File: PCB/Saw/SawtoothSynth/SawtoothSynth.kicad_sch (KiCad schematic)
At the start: 35 parts, among them Q1 SS8550, U1 NE555D, U2 LM358, U3 LM386, U4 L7805, U5 4017

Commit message: Added ESP32 & TFT Display to Schematic
Created footprints and added display and ESP32 to schematic with their respective connections
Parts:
- added RoundDispTFT1: ~, DIsplay:1.28__Round_TFT, symbol Display:1.28{dblquote}_Round_TFT
- added U6: ~, Micro Dev Kits:ESP32-WROOM_Devkit, symbol PCM_Espressif:ESP32-WROOM_Devkit
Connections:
- net +5V: now also RoundDispTFT1.1 (Vcc), U6.2 (VIN)
- net DAC: now also U6.10 (DAC_1/ADC2_CH8/GPIO25)
- net GND: now also RoundDispTFT1.2 (GND), U6.1 (GND), U6.15 (GND), U6.38 (GND), U6.39 (GND_THERMAL)
- net SAWTOOTH_MICRO: now reaches R5.2, R6.1, U2.5 (+)
- net SAWTOOTH_MICRO: now also U6.4 (SENSOR_VP/GPIO36/ADC1_CH0)
- new net SPI_CS: RoundDispTFT1.6 (CS), U6.24 (ADC2_CH2/TOUCH/GPIO2)
- new net SPI_DC: RoundDispTFT1.5 (DC), U6.35 (U0TXD/GPIO1)
- new net SPI_MOSI: RoundDispTFT1.4 (SDA), U6.37 (GPIO23)
- new net SPI_RST: RoundDispTFT1.7 (RST), U6.34 (U0RXD/GPIO3)
- new net SPI_SCK: RoundDispTFT1.3 (SCL), U6.30 (GPIO18)
- new net TOUCH: U6.26 (ADC2_CH0/TOUCH/GPIO4)
- no-connect marks 0 -> 1
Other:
- note added: "2.8" TFT Display"
- note added: "ESP32-WROOM Development Kit"

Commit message: Finished Laying Out Schematic
Added all components, footprints, symbols.

Swapped Voltage Regulator to LD1117S50TR due to smaller footprint
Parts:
- removed C6: 250nF, symbol Device:C_Polarized_Small_US
- removed RV1, RV2: 10K, symbol Device:R_Potentiometer
- removed U4: L7805, symbol Regulator_Linear:L7805
- added C6: 220nF, CustomLibrary:25THV220M8X10.5, symbol CustomLibrary:25THV220M8X10.5
- added C8: 25THV220M8X10.5, CAP_J-V_8X10P5_RUB, symbol CustomLibrary:25THV220M8X10.5
- added RV1, RV2: 10K, CustomLibrary:TRIM_TC33X-2-103E, symbol CustomLibrary:TRIM_TC33X-2-103E
- added U7: LD1117S50TR_SOT223, Package_TO_SOT_SMD:SOT-223-3_TabPin2, symbol Regulator_Linear:LD1117S50TR_SOT223
- C1: value C_Small -> 100nF; footprint (none) -> Capacitor_SMD:C_0805_2012Metric
- C2, C3, C7: value C_Small -> 10nF; footprint (none) -> Capacitor_SMD:C_0805_2012Metric
- C4: footprint (none) -> Capacitor_SMD:C_0805_2012Metric
- C5: value C_Small -> 47nF; footprint (none) -> Capacitor_SMD:C_0805_2012Metric
- LS1: footprint (none) -> Connector_PinHeader_2.54mm:PinHeader_1x02_P2.54mm_Vertical
- R1: value R_US -> 100; footprint (none) -> Resistor_SMD:R_0805_2012Metric
- R2, R4: value R_US -> 10K; footprint (none) -> Resistor_SMD:R_0805_2012Metric
- R3: value R_US -> 33K; footprint (none) -> Resistor_SMD:R_0805_2012Metric
- R5: value R_US -> 100K; footprint (none) -> Resistor_SMD:R_0805_2012Metric
- R6: value R_US -> 6.8K; footprint (none) -> Resistor_SMD:R_0805_2012Metric
- R7: value R_US -> 10; footprint (none) -> Resistor_SMD:R_0805_2012Metric
- R8: footprint (none) -> Resistor_SMD:R_0805_2012Metric
- RoundDispTFT1: footprint DIsplay:1.28__Round_TFT -> CustomLibrary:1.28___Round_TFT
- U2: footprint (none) -> CustomLibrary:LM358DR2G
- U3: footprint (none) -> CustomLibrary:LM386MX-1NOPB
- U5: footprint (none) -> CustomLibrary:CD4017BM96
- U6: footprint Micro Dev Kits:ESP32-WROOM_Devkit -> CustomLibrary:ESP32-WROOM_Devkit
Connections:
- net +12V: now also U7.3 (VI)
- net GND: now also RV1.3, U7.1 (GND)
- net at U2.6 (-), U2.7: now also RV2.1
- net at U3.3 (+): now also RV2.2
- net at C5.2, U3.5: now also C6.1
- net at LS1.1: now also C6.2
- net at C7.1: now also U7.2 (VO)
- net at R1.2: now also RV1.2

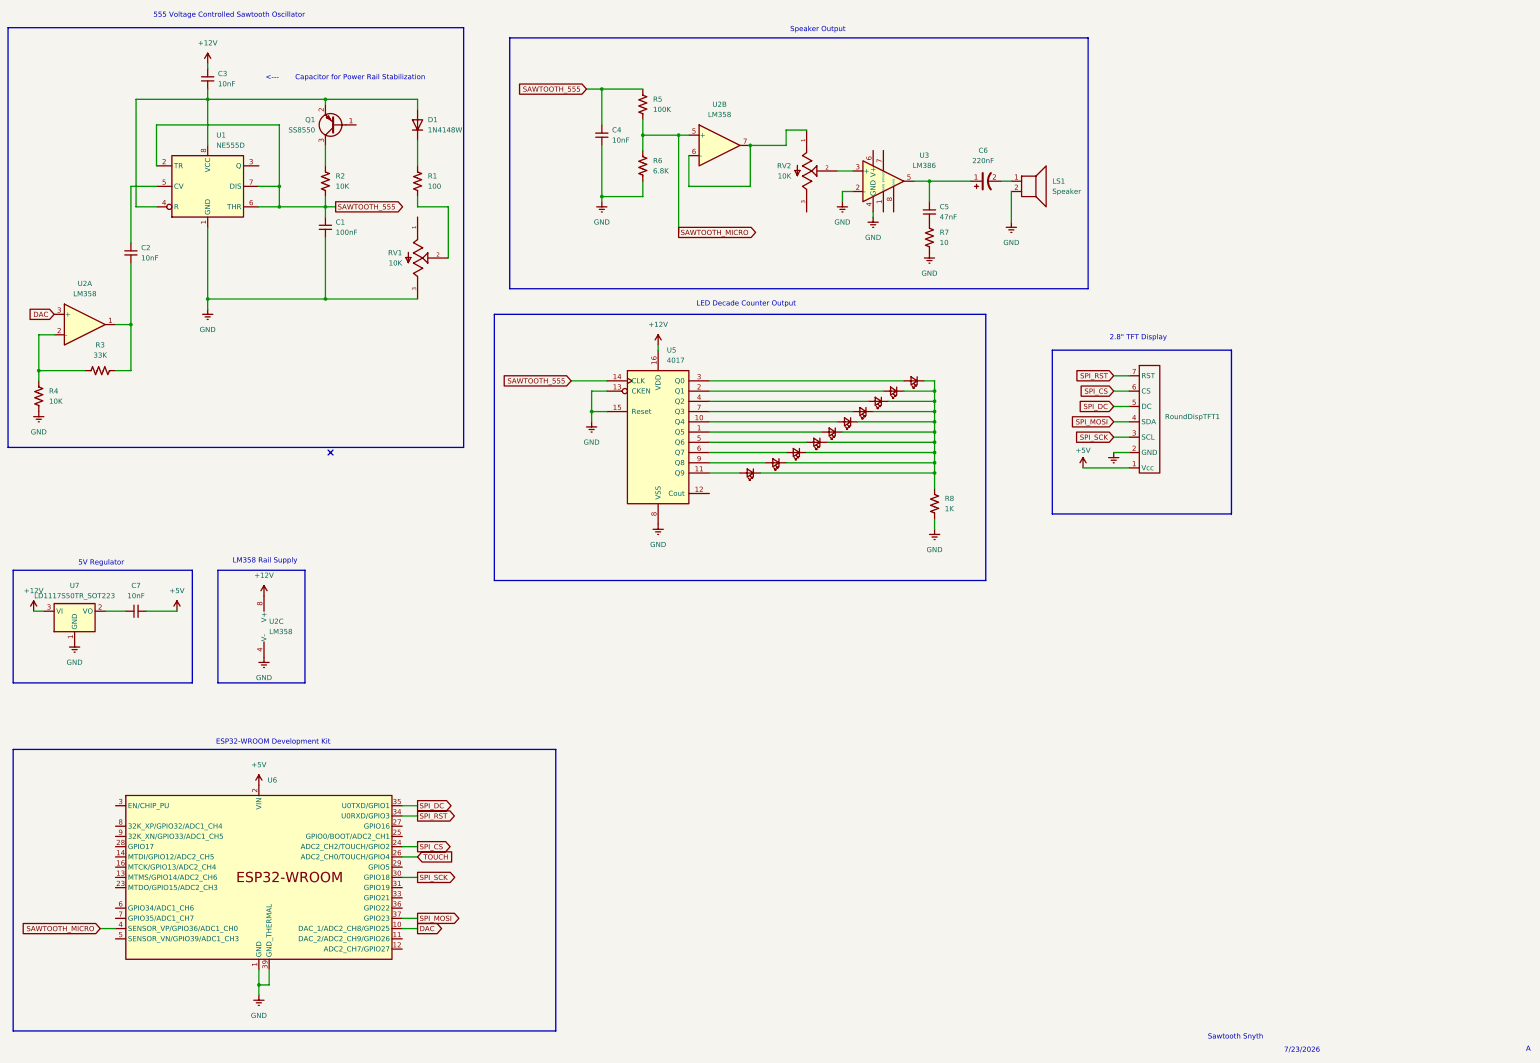
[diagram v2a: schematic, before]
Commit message: Added LED Footprint & Battery Holder
Selected 0805 Footprint for LED and added A23 battery holder to schematic
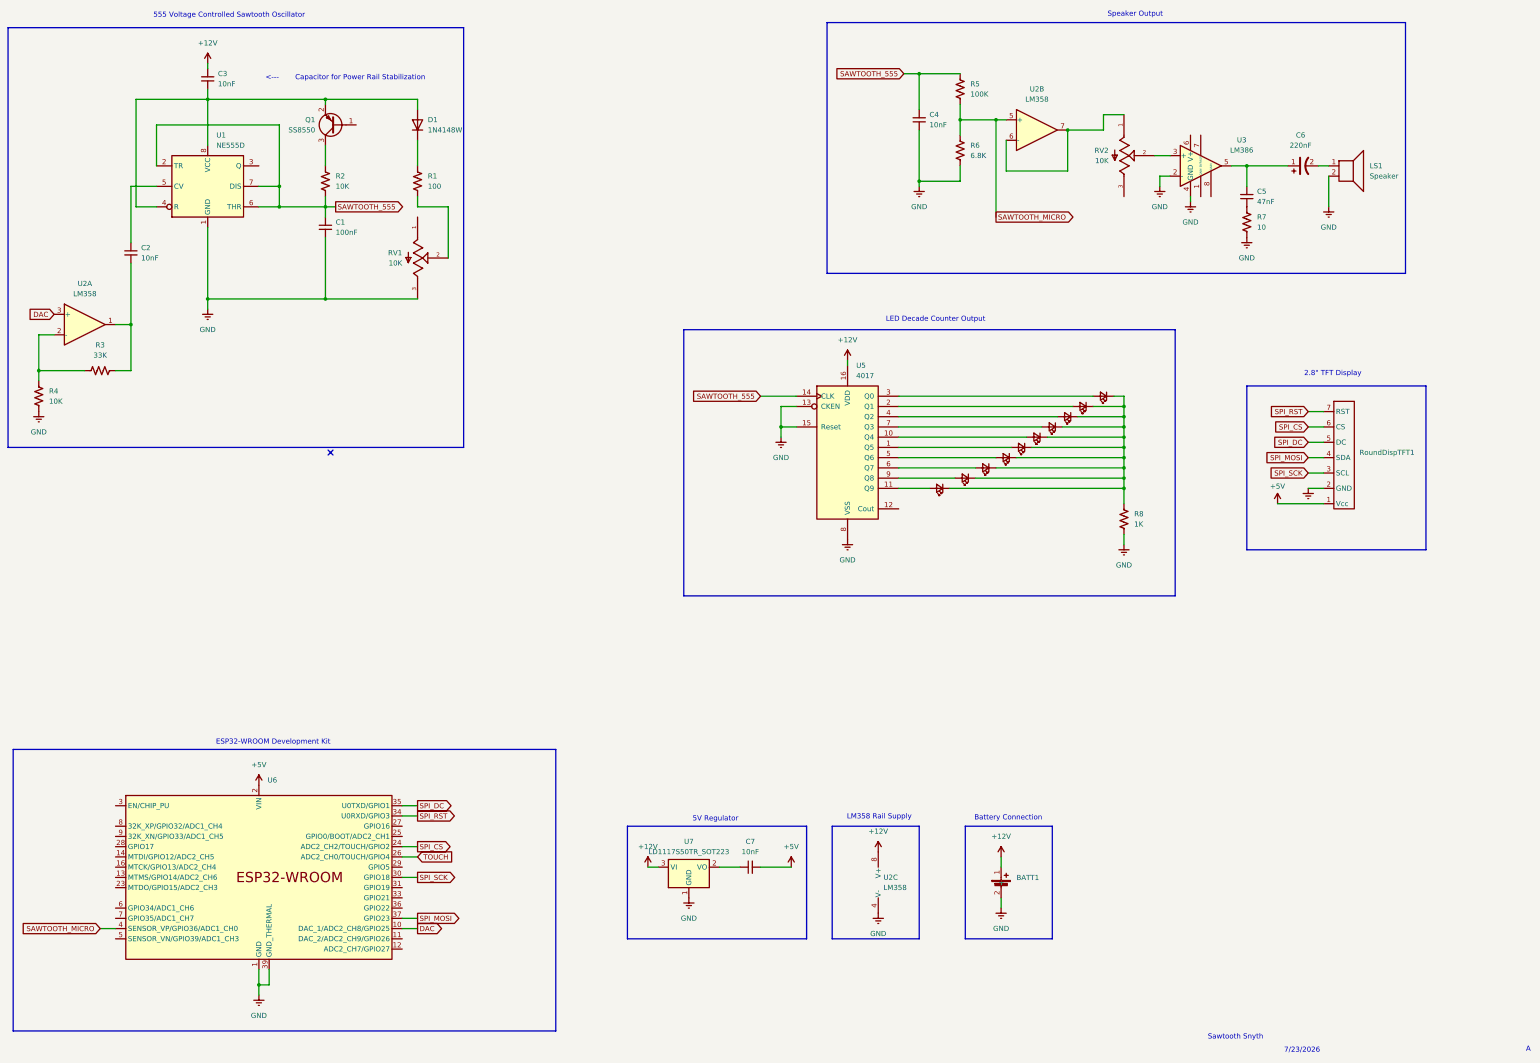
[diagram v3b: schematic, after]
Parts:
- added BATT1: ~, CustomLibrary:BH23APC, symbol CustomLibrary:BH23APC
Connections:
- net +12V: now also BATT1.1 (+)
- net GND: now also BATT1.2 (-)
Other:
- note added: "Battery Connection"
- moved on the sheet: C4, C5, C6, C7, LS1, R5, R6, R7, R8, RV2, RoundDispTFT1, U2B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

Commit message: Created PCB, Updated Schematic
Created an 4 layer, 8 inch PCB
- 2 signal layers, one power, one ground

Last commit I stated that I added the footprint for the LED which was wrong. Updated them correctly in this commit.

Moved capacitor for smoothing the power rail to the positive pin on the battery
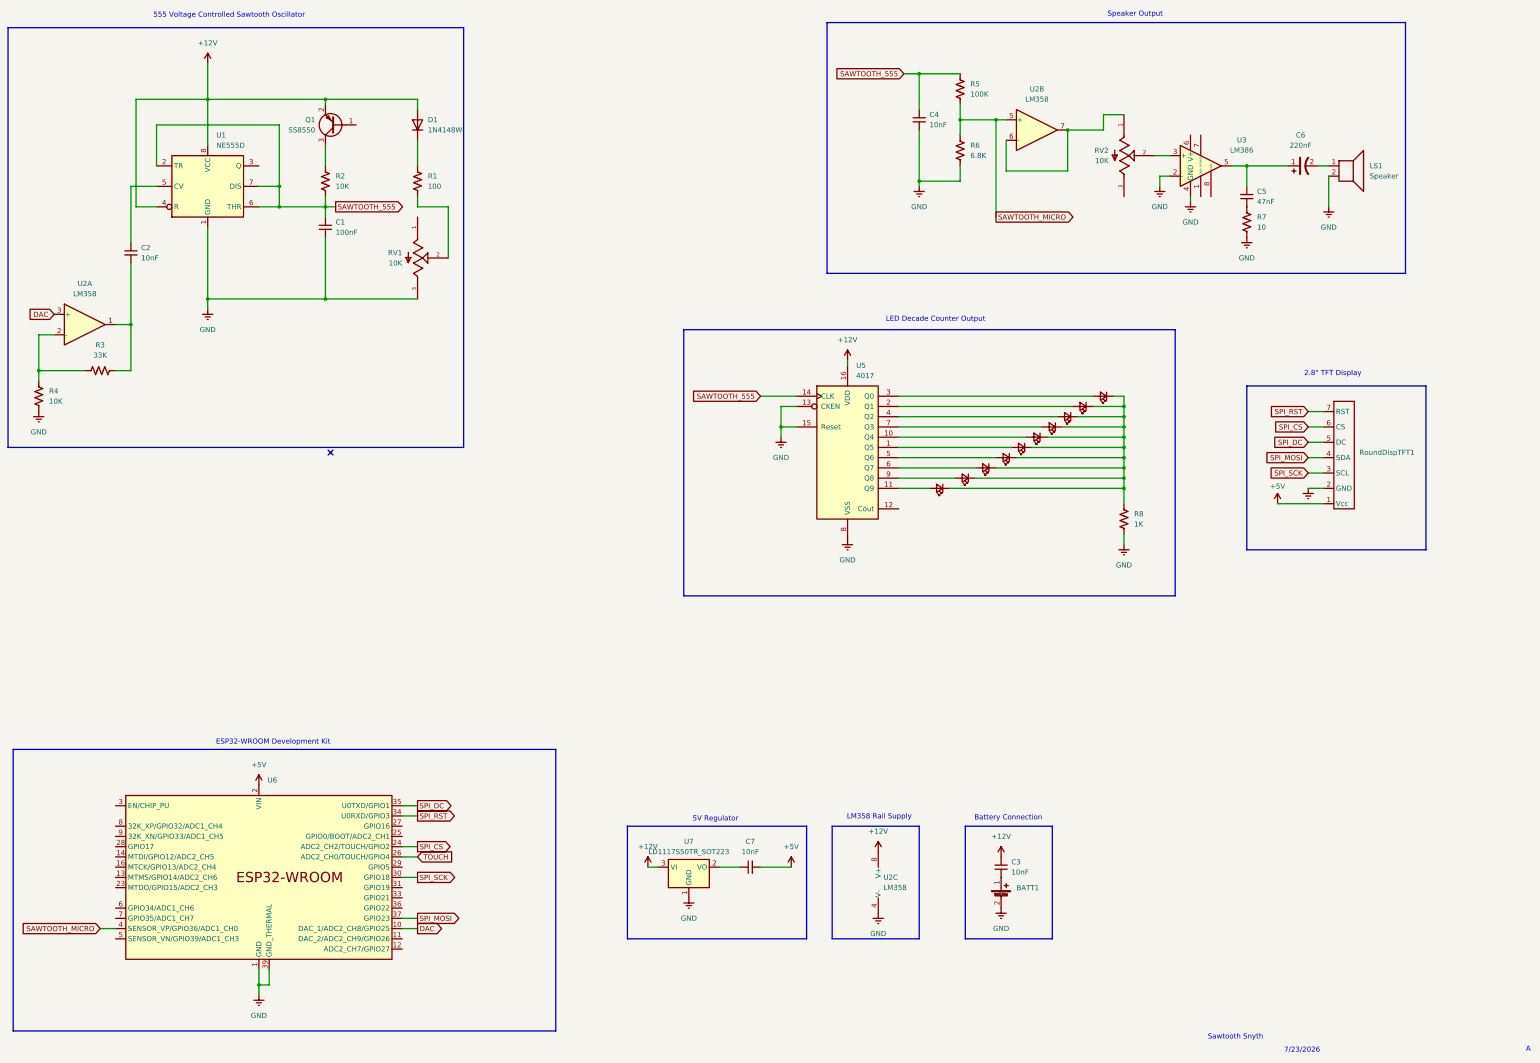
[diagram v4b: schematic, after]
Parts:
- D10, D11, D2, D3, D4, D5, D6, D7, D8, D9: footprint (none) -> LED_SMD:LED_0805_2012Metric_Pad1.15x1.40mm_HandSolder
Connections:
- net +12V: now also D1.2 (A), Q1.2 (E), U1.4 (R), U1.8 (VCC); no longer BATT1.1 (+)
- new net: BATT1.1 (+), C3.1
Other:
- note removed: "<---"
- note removed: "Capacitor for Power Rail Stabilization"
- moved on the sheet: BATT1, C3
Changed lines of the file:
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@@
 		)
 	)
-	(text "<---"
-		(exclude_from_sim no)
-		(at 80.772 39.116 0)
-		(effects
-			(font
-				(size 1.27 1.27)
-			)
-		)
-	)
 	(text "ESP32-WROOM Development Kit\n"
 		(exclude_from_sim no)
@@
 		)
 	)
-	(text "Capacitor for Power Rail Stabilization\n"
-		(exclude_from_sim no)
-		(at 102.616 39.116 0)
-		(effects
-			(font
-				(size 1.27 1.27)
-			)
-		)
-	)
 	(text "7/23/2026\n"
 		(exclude_from_sim no)
@@
 	(wire
 		(pts
-			(xy 261.62 242.57) (xy 261.62 245.11)
-		)
-		(stroke
-			(width 0)
-			(type default)
-		)
-	)
-	(wire
-		(pts
 			(xy 236.22 118.11) (xy 284.48 118.11)
 		)
@@
 	(wire
 		(pts
-			(xy 52.07 66.04) (xy 45.72 66.04)
+			(xy 64.77 35.56) (xy 64.77 44.45)
 		)
 		(stroke
@@
 	(wire
 		(pts
-			(xy 292.1 152.4) (xy 292.1 154.94)
+			(xy 52.07 66.04) (xy 45.72 66.04)
 		)
 		(stroke
@@
 	(wire
 		(pts
-			(xy 237.49 38.1) (xy 241.3 38.1)
+			(xy 292.1 152.4) (xy 292.1 154.94)
 		)
 		(stroke
@@
 	(wire
 		(pts
-			(xy 278.13 52.07) (xy 287.02 52.07)
+			(xy 237.49 38.1) (xy 241.3 38.1)
 		)
 		(stroke
@@
 	(wire
 		(pts
-			(xy 201.93 118.11) (xy 210.82 118.11)
+			(xy 278.13 52.07) (xy 287.02 52.07)
 		)
 		(stroke
@@
 	(wire
 		(pts
-			(xy 337.82 140.97) (xy 341.63 140.97)
+			(xy 201.93 118.11) (xy 210.82 118.11)
 		)
 		(stroke
@@
 	(wire
 		(pts
-			(xy 292.1 123.19) (xy 292.1 125.73)
+			(xy 337.82 140.97) (xy 341.63 140.97)
 		)
 		(stroke
@@
 	(wire
 		(pts
-			(xy 64.77 35.56) (xy 64.77 36.83)
+			(xy 292.1 123.19) (xy 292.1 125.73)
 		)
 		(stroke
@@
 	(wire
 		(pts
-			(xy 261.62 232.41) (xy 261.62 234.95)
-		)
-		(stroke
-			(width 0)
-			(type default)
-		)
-	)
-	(wire
-		(pts
 			(xy 113.03 247.65) (xy 116.84 247.65)
 		)
@@
 	(wire
 		(pts
-			(xy 64.77 41.91) (xy 64.77 44.45)
-		)
-		(stroke
-			(width 0)
-			(type default)
-		)
-	)
-	(wire
-		(pts
 			(xy 93.98 71.12) (xy 93.98 73.66)
 		)
@@
 	(symbol
 		(lib_id "Device:C_Small")
-		(at 64.77 39.37 180)
+		(at 261.62 234.95 180)
 		(unit 1)
 		(exclude_from_sim no)
@@
 		(fields_autoplaced yes)
 		(property "Reference" "C3"
-			(at 67.31 38.0935 0)
+			(at 264.16 233.6735 0)
 			(effects
 				(font
@@
 		)
 		(property "Value" "10nF"
-			(at 67.31 40.6335 0)
+			(at 264.16 236.2135 0)
 			(effects
 				(font
@@
 		)
 		(property "Footprint" "Capacitor_SMD:C_0805_2012Metric"
-			(at 64.77 39.37 0)
+			(at 261.62 234.95 0)
 			(effects
 				(font
@@
 		)
 		(property "Datasheet" "~"
-			(at 64.77 39.37 0)
+			(at 261.62 234.95 0)
 			(effects
 				(font
@@
 		)
 		(property "Description" "Unpolarized capacitor, small symbol"
-			(at 64.77 39.37 0)
+			(at 261.62 234.95 0)
 			(effects
 				(font
@@
 	(symbol
 		(lib_id "CustomLibrary:BH23APC")
-		(at 257.81 238.76 270)
+		(at 257.81 241.3 270)
 		(unit 1)
 		(exclude_from_sim no)
@@
 		(fields_autoplaced yes)
 		(property "Reference" "BATT1"
-			(at 265.43 237.5534 90)
+			(at 265.43 240.0934 90)
 			(effects
 				(font
@@
 		)
 		(property "Value" "~"
-			(at 265.43 239.4585 90)
+			(at 265.43 241.9985 90)
 			(effects
 				(font
@@
 		)
 		(property "Footprint" "CustomLibrary:BH23APC"
-			(at 257.81 238.76 0)
+			(at 257.81 241.3 0)
 			(effects
 				(font
@@
 		)
 		(property "Datasheet" ""
-			(at 257.81 238.76 0)
+			(at 257.81 241.3 0)
 			(effects
 				(font
@@
 		)
 		(property "Description" ""
-			(at 257.81 238.76 0)
+			(at 257.81 241.3 0)
 			(effects
 				(font
@@
 			)
 		)
-		(property "Footprint" ""
+		(property "Footprint" "LED_SMD:LED_0805_2012Metric_Pad1.15x1.40mm_HandSolder"
 			(at 278.13 123.19 90)
 			(effects
@@
 			)
 		)
-		(property "Footprint" ""
+		(property "Footprint" "LED_SMD:LED_0805_2012Metric_Pad1.15x1.40mm_HandSolder"
 			(at 287.02 118.11 90)
 			(effects
@@
 			)
 		)
-		(property "Footprint" ""
+		(property "Footprint" "LED_SMD:LED_0805_2012Metric_Pad1.15x1.40mm_HandSolder"
 			(at 252.73 138.43 90)
 			(effects
@@
 			)
 		)
-		(property "Footprint" ""
+		(property "Footprint" "LED_SMD:LED_0805_2012Metric_Pad1.15x1.40mm_HandSolder"
 			(at 246.38 140.97 90)
 			(effects
@@
 			)
 		)
-		(property "Footprint" ""
+		(property "Footprint" "LED_SMD:LED_0805_2012Metric_Pad1.15x1.40mm_HandSolder"
 			(at 274.32 125.73 90)
 			(effects
@@
 			)
 		)
-		(property "Footprint" ""
+		(property "Footprint" "LED_SMD:LED_0805_2012Metric_Pad1.15x1.40mm_HandSolder"
 			(at 262.89 133.35 90)
 			(effects
@@
 			)
 		)
-		(property "Footprint" ""
+		(property "Footprint" "LED_SMD:LED_0805_2012Metric_Pad1.15x1.40mm_HandSolder"
 			(at 257.81 135.89 90)
 			(effects
@@
 			)
 		)
-		(property "Footprint" ""
+		(property "Footprint" "LED_SMD:LED_0805_2012Metric_Pad1.15x1.40mm_HandSolder"
 			(at 281.94 120.65 90)
 			(effects
@@
 			)
 		)
-		(property "Footprint" ""
+		(property "Footprint" "LED_SMD:LED_0805_2012Metric_Pad1.15x1.40mm_HandSolder"
 			(at 266.7 130.81 90)
 			(effects
@@
 			)
 		)
-		(property "Footprint" ""
+		(property "Footprint" "LED_SMD:LED_0805_2012Metric_Pad1.15x1.40mm_HandSolder"
 			(at 270.51 128.27 90)
 			(effects
